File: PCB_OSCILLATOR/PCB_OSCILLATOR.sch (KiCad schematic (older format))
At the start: 72 parts, among them P1 POWER SUPPLY, P2 SPI_AD5270_1, P3 SPI_AD5270_2, P4 SPI_AD9833_1, P5 SPI_AD9833_2, U1 AD5270, U2 AD8421, U3 AD9833, U4 AD5270, U5 AD8421, U6 AD9833, U7 ADG819

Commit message: Primera Versión completa con diagrama de bloques en carpeta principal
//
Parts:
- removed R1, R10, R11, R2, R3, R4, R5, R6, R7, R8, R9: 0R, Resistors_SMD:R_0805_HandSoldering, symbol R_Small
- removed W1: TEST_8, Measurement_Points:Measurement_Point_Round-TH_Small, symbol TEST_1P
- removed W3: TEST_9, Measurement_Points:Measurement_Point_Round-TH_Small, symbol TEST_1P
- removed W5: TEST_10, Measurement_Points:Measurement_Point_Round-TH_Small, symbol TEST_1P
- removed W7: TEST_11, Measurement_Points:Measurement_Point_Round-TH_Small, symbol TEST_1P
- removed W9: TEST_12, Measurement_Points:Measurement_Point_Round-TH_Small, symbol TEST_1P
- added J1, J10, J11, J2, J3, J4, J5, J6, J7, J8, J9: Jumper, Pin_Headers:Pin_Header_Straight_1x02, symbol Jumper
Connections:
- wire segments 211 -> 206
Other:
- note added: "Falta pedir los reguladores de 3, 5, 18 y -18.\nY poner regulador 5"
- moved on the sheet: C28, C29, W10, W12, W14, W2, W4, W6, W8

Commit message: SEGREGANDO ELEMENTOS SIN VER CAMINOS NI CAPACITORES
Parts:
- P1: footprint Pin_Headers:Pin_Header_Angled_1x05 -> Socket_Strips:Socket_Strip_Straight_1x05
- P2, P3, P4, P5: footprint Socket_Strips:Socket_Strip_Angled_1x06 -> Socket_Strips:Socket_Strip_Straight_1x06
- U1, U3, U4, U6: footprint Housings_SSOP:MSOP-10-1EP_3x3mm_Pitch0.5mm -> Housings_SSOP:MSOP-10_3x3mm_Pitch0.5mm
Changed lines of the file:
@@
 F 0 "U3" H 2600 2270 60  0000 C CNN
 F 1 "AD9833" H 2590 1870 60  0000 C CNN
-F 2 "Housings_SSOP:MSOP-10-1EP_3x3mm_Pitch0.5mm" H 2420 2030 60  0001 C CNN
+F 2 "Housings_SSOP:MSOP-10_3x3mm_Pitch0.5mm" H 2420 2030 60  0001 C CNN
 F 3 "" H 2420 2030 60  0000 C CNN
 	1    2620 2000
@@
 F 0 "U6" H 5650 2240 60  0000 C CNN
 F 1 "AD9833" H 5640 1840 60  0000 C CNN
-F 2 "Housings_SSOP:MSOP-10-1EP_3x3mm_Pitch0.5mm" H 5470 2000 60  0001 C CNN
+F 2 "Housings_SSOP:MSOP-10_3x3mm_Pitch0.5mm" H 5470 2000 60  0001 C CNN
 F 3 "" H 5470 2000 60  0000 C CNN
 	1    5670 1970
@@
 F 0 "U1" H 1800 6460 60  0000 C CNN
 F 1 "AD5270" H 2090 5950 60  0000 C CNN
-F 2 "Housings_SSOP:MSOP-10-1EP_3x3mm_Pitch0.5mm" H 2190 6080 60  0001 C CNN
+F 2 "Housings_SSOP:MSOP-10_3x3mm_Pitch0.5mm" H 2190 6080 60  0001 C CNN
 F 3 "" H 2190 6080 60  0000 C CNN
 	1    1560 6170
@@
 F 0 "U4" H 4590 6470 60  0000 C CNN
 F 1 "AD5270" H 4880 5960 60  0000 C CNN
-F 2 "Housings_SSOP:MSOP-10-1EP_3x3mm_Pitch0.5mm" H 4980 6090 60  0001 C CNN
+F 2 "Housings_SSOP:MSOP-10_3x3mm_Pitch0.5mm" H 4980 6090 60  0001 C CNN
 F 3 "" H 4980 6090 60  0000 C CNN
 	1    4350 6180
@@
 F 0 "P2" H 8010 1370 50  0000 C CNN
 F 1 "SPI_AD5270_1" V 8110 1020 50  0000 C CNN
-F 2 "Socket_Strips:Socket_Strip_Angled_1x06" H 8010 1020 50  0001 C CNN
+F 2 "Socket_Strips:Socket_Strip_Straight_1x06" H 8010 1020 50  0001 C CNN
 F 3 "" H 8010 1020 50  0000 C CNN
 	1    8010 1020
@@
 F 0 "P3" H 8850 1370 50  0000 C CNN
 F 1 "SPI_AD5270_2" V 8950 1020 50  0000 C CNN
-F 2 "Socket_Strips:Socket_Strip_Angled_1x06" H 8850 1020 50  0001 C CNN
+F 2 "Socket_Strips:Socket_Strip_Straight_1x06" H 8850 1020 50  0001 C CNN
 F 3 "" H 8850 1020 50  0000 C CNN
 	1    8850 1020
@@
 F 0 "P4" H 9610 1370 50  0000 C CNN
 F 1 "SPI_AD9833_1" V 9710 1020 50  0000 C CNN
-F 2 "Socket_Strips:Socket_Strip_Angled_1x06" H 9610 1020 50  0001 C CNN
+F 2 "Socket_Strips:Socket_Strip_Straight_1x06" H 9610 1020 50  0001 C CNN
 F 3 "" H 9610 1020 50  0000 C CNN
 	1    9610 1020
@@
 F 0 "P5" H 10360 1360 50  0000 C CNN
 F 1 "SPI_AD9833_2" V 10460 1010 50  0000 C CNN
-F 2 "Socket_Strips:Socket_Strip_Angled_1x06" H 10360 1010 50  0001 C CNN
+F 2 "Socket_Strips:Socket_Strip_Straight_1x06" H 10360 1010 50  0001 C CNN
 F 3 "" H 10360 1010 50  0000 C CNN
 	1    10360 1010
@@
 F 0 "P1" H 7970 2810 50  0000 C CNN
 F 1 "POWER SUPPLY" V 8070 2510 50  0000 C CNN
-F 2 "Pin_Headers:Pin_Header_Angled_1x05" H 7970 2510 50  0001 C CNN
+F 2 "Socket_Strips:Socket_Strip_Straight_1x05" H 7970 2510 50  0001 C CNN
 F 3 "" H 7970 2510 50  0000 C CNN
 	1    7970 2510

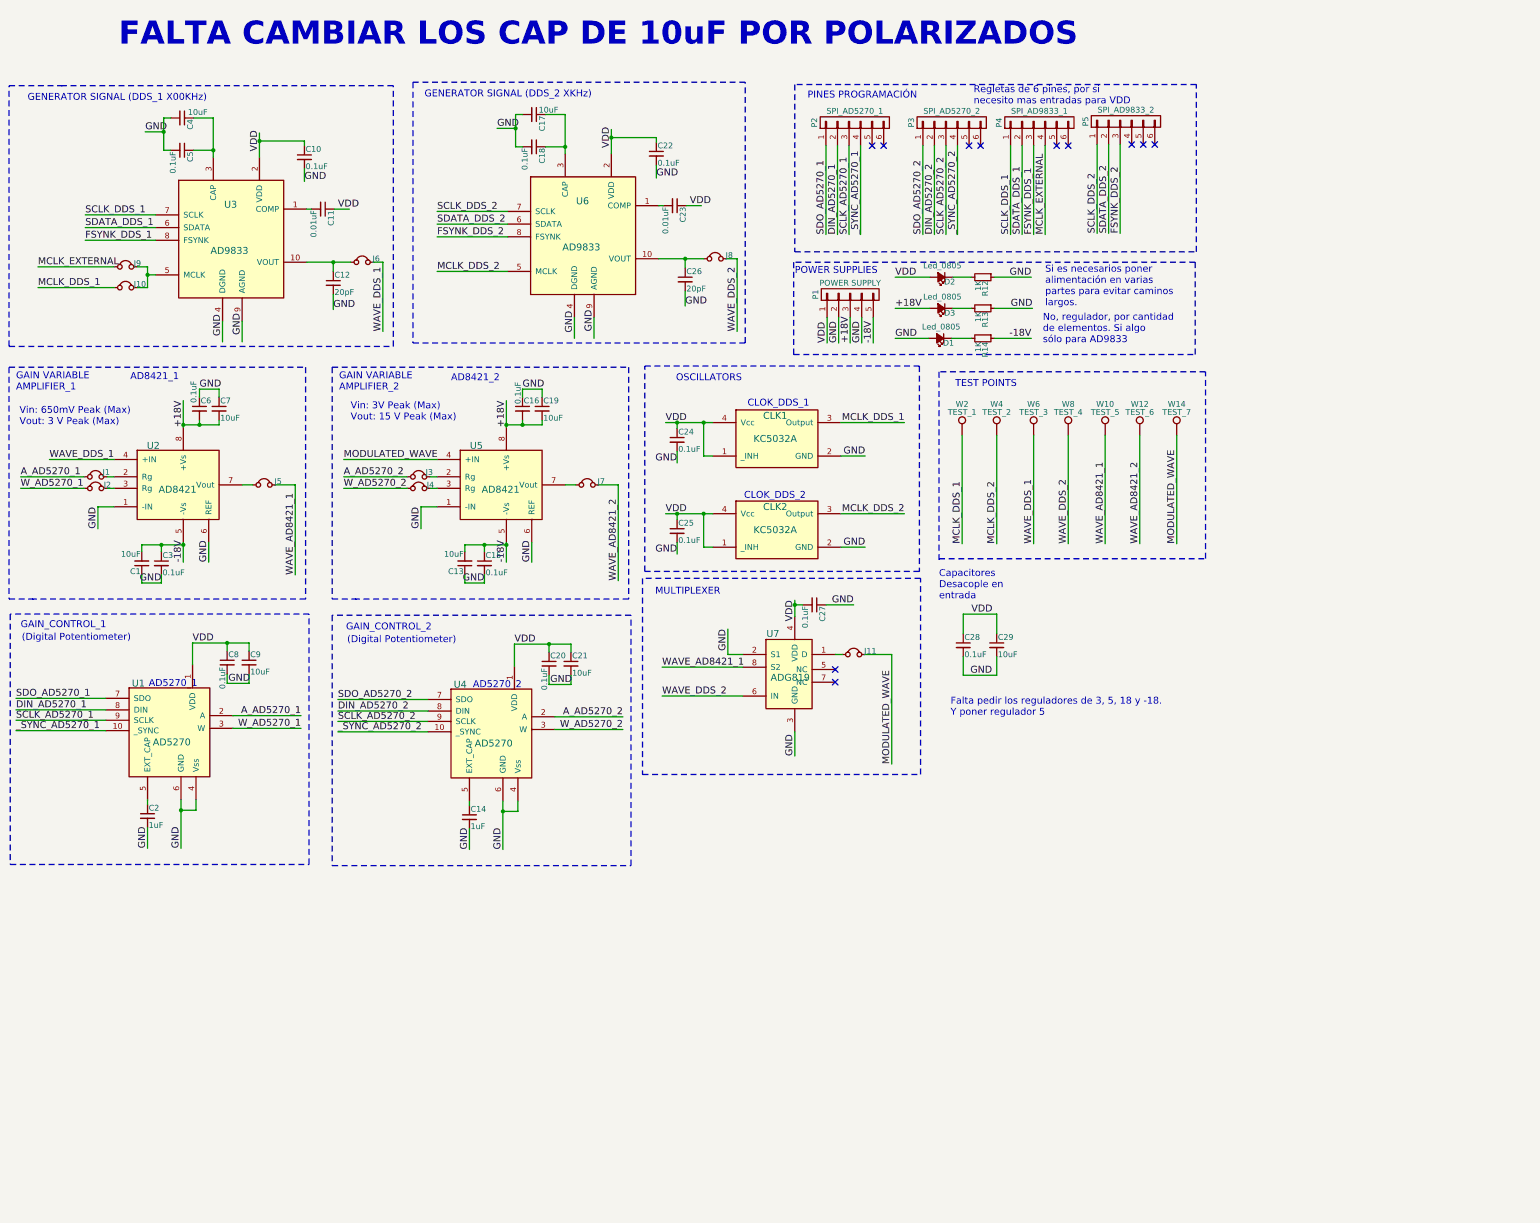
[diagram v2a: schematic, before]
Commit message: Faltan Hacer correciones que están en trello
Terminar correciones y pasar a la etapa de segregación de elementos,
layout final propuesto para el viernes 12
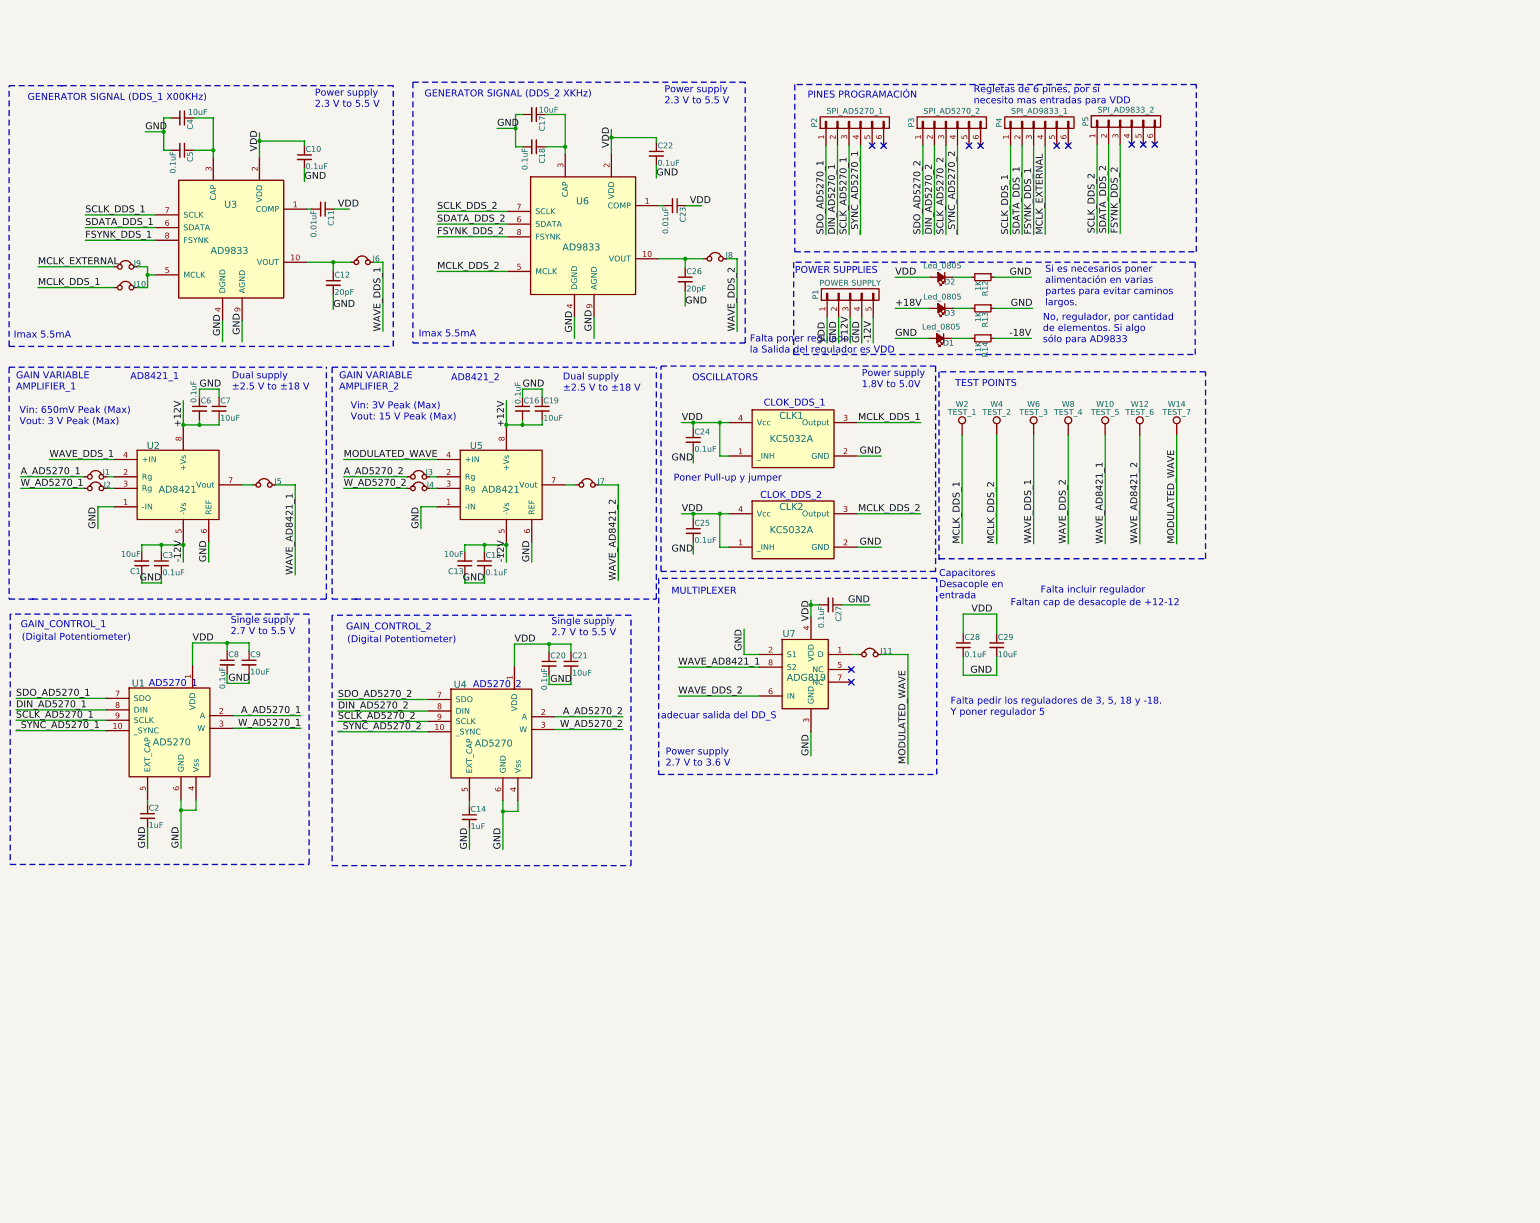
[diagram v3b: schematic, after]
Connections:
- net labels added: +12V, -12V
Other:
- note added: "Dual supply\n±2.5 V to ±18 V"
- note added: "Falta incluir regulador"
- note added: "Falta poner regulador\nla Salida del regulador es VDD"
- note added: "Faltan cap de desacople de +12-12"
- note added: "Imax 5.5mA"
- note added: "Poner Pull-up y jumper"
- note added: "Power supply\n1.8V to 5.0V"
- note added: "Power supply\n2.3 V to 5.5 V"
- note added: "Power supply\n2.7 V to 3.6 V"
- note added: "Single supply\n2.7 V to 5.5 V"
- note added: "adecuar salida del DD_S"
- note removed: "FALTA CAMBIAR LOS CAP DE 10uF POR POLARIZADOS"
- moved on the sheet: C24, C25, C27, CLK1, CLK2, J11, U7

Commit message: Algunos cambios Adicionales
//
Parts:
- added C30: 1uF, Capacitors_SMD:C_0805_HandSoldering, symbol 1uF
- added C31: 0.47uF, Capacitors_SMD:C_1206_HandSoldering, symbol 0.47uF
- added C32, C33, C35, C37, C39: 0.1uF, Resistors_SMD:R_0805_HandSoldering, symbol 0.1uF
- added C34, C36, C38: 10uF, Resistors_SMD:R_0805_HandSoldering, symbol 10uF
- added J12, J13, J14, J15, J16: Jumper, Pin_Headers:Pin_Header_Straight_1x02, symbol Jumper
- added R1, R3: 1K, Resistors_SMD:R_0805_HandSoldering, symbol 1K
- added R2: 100K, Resistors_SMD:R_0805_HandSoldering, symbol 100K
- added R4: 10K, Resistors_SMD:R_0805_HandSoldering, symbol 10K
- added U10: ADR291, TO_SOT_Packages_THT:TO-92_Inline_Narrow_Oval, symbol ADR291
- added U8: ADP3303, Housings_SOIC:SOIC-8_3.9x4.9mm_Pitch1.27mm, symbol ADP3303
- added U9: AD8651, Housings_SOIC:SOIC-8_3.9x4.9mm_Pitch1.27mm, symbol AD8651
- added W1: TEST_8, Measurement_Points:Measurement_Point_Round-TH_Small, symbol TEST_1P
- added W11: TEST_13, Measurement_Points:Measurement_Point_Round-TH_Small, symbol TEST_1P
- added W13: TEST_14, Measurement_Points:Measurement_Point_Round-TH_Small, symbol TEST_1P
- added W3: TEST_9, Measurement_Points:Measurement_Point_Round-TH_Small, symbol TEST_1P
- added W5: TEST_10, Measurement_Points:Measurement_Point_Round-TH_Small, symbol TEST_1P
- added W7: TEST_11, Measurement_Points:Measurement_Point_Round-TH_Small, symbol TEST_1P
- added W9: TEST_12, Measurement_Points:Measurement_Point_Round-TH_Small, symbol TEST_1P
- C1, C13, C19, C7: footprint Resistors_SMD:R_0805_HandSoldering -> Capacitors_SMD:C_1206_HandSoldering; 25V 490-5523-2-ND -> (none); CAP TANT 10UF 16V 10% 1206 (none) -> 478-8235-2-ND
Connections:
- net labels added: +5V, BASE_WAVE, FINAL_WAVE, MODULATING_WAVE, REF_0.25V, REF_2.5V
- net labels removed: +18V, -18V, WAVE_AD8421_1, WAVE_AD8421_2
- wire segments 206 -> 268
- no-connect marks 11 -> 13
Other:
- note added: "CLOCK LEVEL ADAPTER"
- note added: "Imax 1[uA]"
- note added: "Imax 2.3[mA]"
- note added: "Imax 5.5[mA]"
- note added: "Imax 6[mA]X2"
- note added: "Power supply\n1.8 V to 5.5 V"
- note added: "REFERENCE VOLTAGE 2.5V"
- note added: "Regulator"
- note removed: "Capacitores\nDesacople en\nentrada\n"
- note removed: "Falta incluir regulador"
- note removed: "Falta pedir los reguladores de 3, 5, 18 y -18.\nY poner regulador 5"
- note removed: "Falta poner regulador\nla Salida del regulador es VDD"
- note removed: "Faltan cap de desacople de +12-12"
- note removed: "Imax 5.5mA"
- note removed: "No, regulador, por cantidad \nde elementos. Si algo \nsólo para AD9833"
- note removed: "Power supply\n2.7 V to 3.6 V"
- note removed: "Si es necesarios poner \nalimentación en varias \npartes para evitar caminos\nlargos."
- moved on the sheet: C1, C10, C11, C12, C13, C14, C15, C16, C17, C18, C19, C2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
